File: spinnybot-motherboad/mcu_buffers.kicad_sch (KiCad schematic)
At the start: 15 parts, among them Q3 BC846, U4 ICM-20649, U5 ESP32-DEVKITC-32D, U6 SN74AHCT541DW, U7 SN74AHCT541DW

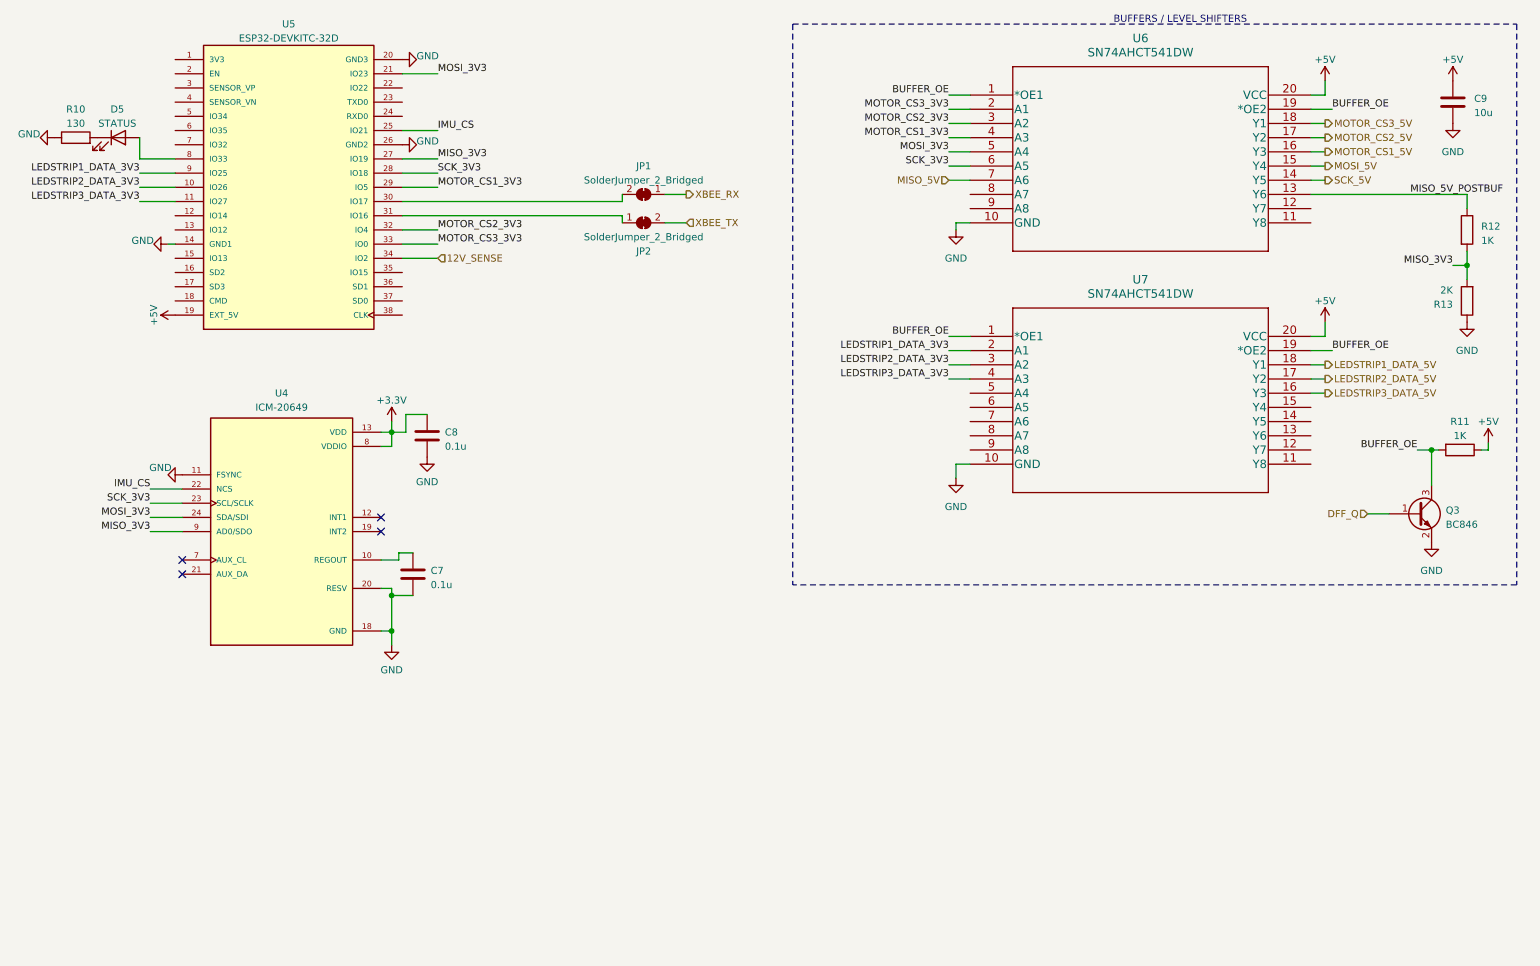
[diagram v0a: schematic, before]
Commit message: routed rev2 mainboard
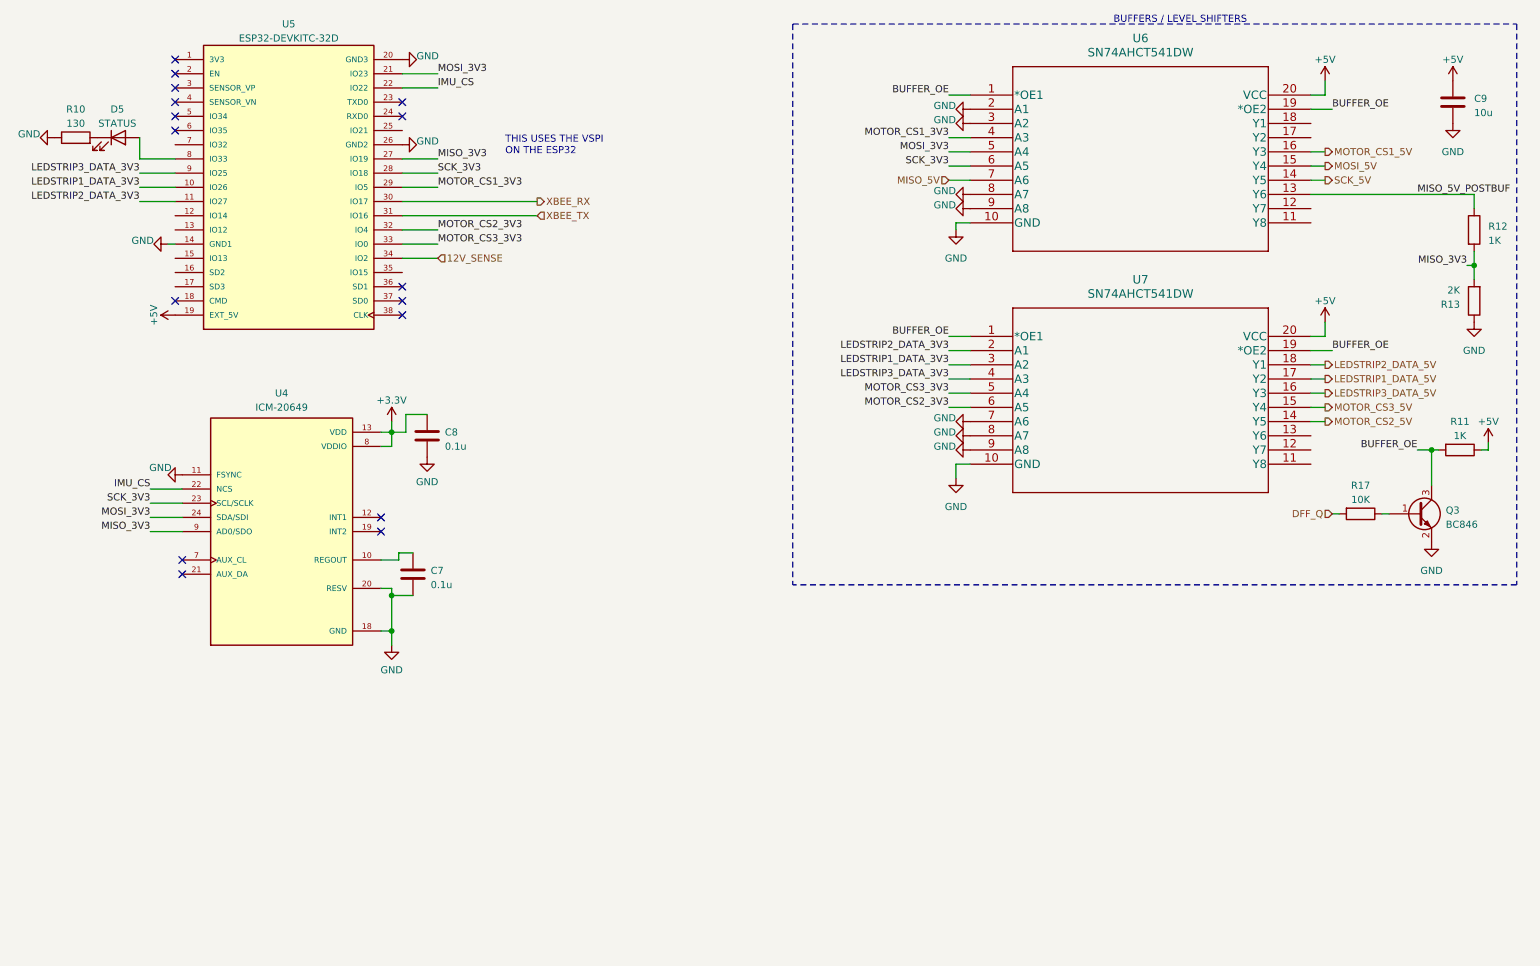
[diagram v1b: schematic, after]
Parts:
- removed JP1, JP2: SolderJumper_2_Bridged, Jumper:SolderJumper-2_P1.3mm_Open_RoundedPad1.0x1.5mm, symbol Jumper:SolderJumper_2_Bridged
- added R17: 10K, Resistor_SMD:R_0805_2012Metric_Pad1.20x1.40mm_HandSolder, symbol Device:R
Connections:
- net DFF_Q: now also R17.2; no longer Q3.1 (B)
- net GND: now also U6.2 (A1), U6.3 (A2), U6.8 (A7), U6.9 (A8), U7.7 (A6), U7.8 (A7), U7.9 (A8)
- net IMU_CS: now also U5.22 (IO22); no longer U5.25 (IO21)
- net LEDSTRIP1_DATA_3V3: now also U5.10 (IO26), U7.3 (A2); no longer U5.9 (IO25), U7.2 (A1)
- net LEDSTRIP1_DATA_5V: now also U7.17 (Y2); no longer U7.18 (Y1)
- net LEDSTRIP2_DATA_3V3: now also U5.11 (IO27), U7.2 (A1); no longer U5.10 (IO26), U7.3 (A2)
- net LEDSTRIP2_DATA_5V: now also U7.18 (Y1); no longer U7.17 (Y2)
- net LEDSTRIP3_DATA_3V3: now also U5.9 (IO25); no longer U5.11 (IO27)
- net MOTOR_CS2_3V3: now also U7.6 (A5); no longer U6.3 (A2)
- net MOTOR_CS2_5V: now also U7.14 (Y5); no longer U6.17 (Y2)
- net MOTOR_CS3_3V3: now also U7.5 (A4); no longer U6.2 (A1)
- net MOTOR_CS3_5V: now also U7.15 (Y4); no longer U6.18 (Y1)
- net XBEE_RX: now also U5.30 (IO17)
- net XBEE_TX: now also U5.31 (IO16)
- new net: Q3.1 (B), R17.1
- no-connect marks 4 -> 16
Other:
- note added: "THIS USES THE VSPI ON THE ESP32"
- moved on the sheet: R12, R13

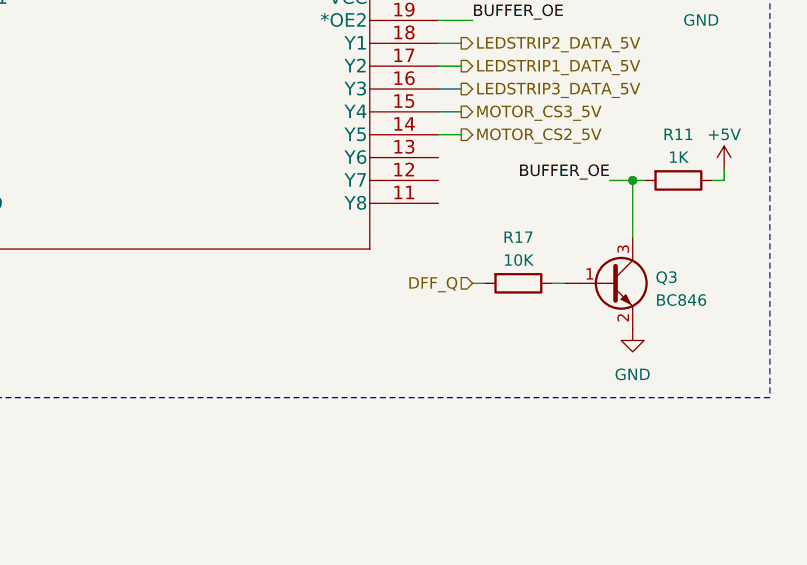
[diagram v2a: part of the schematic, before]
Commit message: split schematic into multiple files and stole Erick's homework on redoing the power button
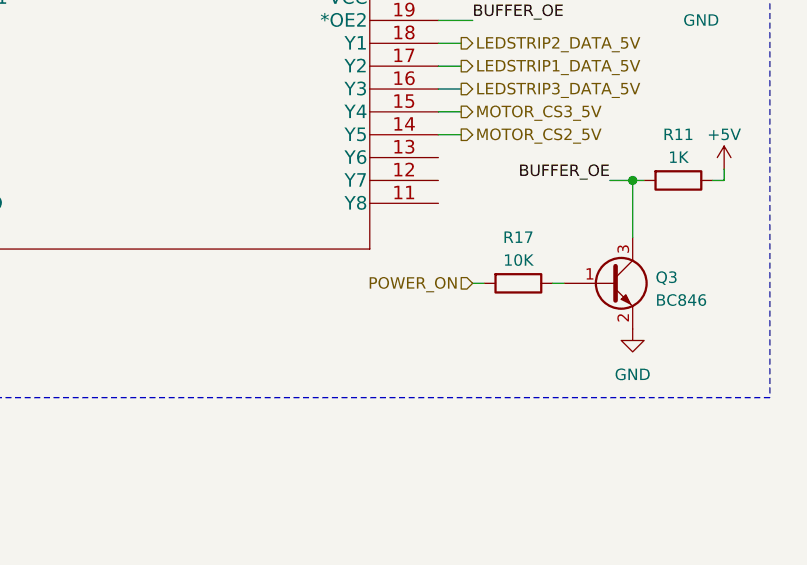
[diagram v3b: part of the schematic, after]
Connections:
- net DFF_Q renamed POWER_ON
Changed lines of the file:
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@@
-(kicad_sch (version 20210621) (generator eeschema)
+(kicad_sch (version 20211123) (generator eeschema)
   (paper "A4")
-  (junction (at 80.645 126.365) (diameter 1.016) (color 0 0 0 0))
-  (junction (at 274.32 60.96) (diameter 1.016) (color 0 0 0 0))
-  (junction (at 80.645 90.805) (diameter 1.016) (color 0 0 0 0))
-  (junction (at 266.7 93.98) (diameter 1.016) (color 0 0 0 0))
-  (junction (at 80.645 120.015) (diameter 1.016) (color 0 0 0 0))
+  (junction (at 266.7 93.98) (diameter 1.016) (color 0 0 0 0)
+  )
+  (junction (at 80.645 90.805) (diameter 1.016) (color 0 0 0 0)
+  )
+  (junction (at 274.32 60.96) (diameter 1.016) (color 0 0 0 0)
+  )
+  (junction (at 80.645 126.365) (diameter 1.016) (color 0 0 0 0)
+  )
+  (junction (at 80.645 120.015) (diameter 1.016) (color 0 0 0 0)
+  )
   (no_connect (at 82.55 64.77))
   (no_connect (at 82.55 67.31))
@@
     (effects (font (size 1.27 1.27)) (justify left))
   )
-  (hierarchical_label "DFF_Q" (shape input) (at 248.92 105.41 180)
+  (hierarchical_label "POWER_ON" (shape input) (at 248.92 105.41 180)
     (effects (font (size 1.27 1.27)) (justify right))
   )

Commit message: fixed some reference designators so the layout isn't broken
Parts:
- added U2: XBP9B-DMWTB002, XBP9-DMWTB002-XBEE-PRO-900HP:DIP2200W51P200L3294H279Q20P, symbol XBP9B-DMWTB002:XBP9B-DMWTB002
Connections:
- net +3V3: now also U2.1 (VCC)
- net GND: now also U2.10 (GND)
- net XBEE_RX: now also U2.3 (DIN/NCONFIG/DIO14)
- net XBEE_TX: now also U2.2 (DOUT/DIO13)
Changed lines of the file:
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@@
     (stroke (width 0) (type solid) (color 0 0 0 0))
+  )
+  (wire (pts (xy 158.75 175.26) (xy 156.21 175.26))
+    (stroke (width 0) (type default) (color 0 0 0 0))
   )
   (wire (pts (xy 180.34 76.2) (xy 184.15 76.2))
@@
     (stroke (width 0) (type solid) (color 0 0 0 0))
   )
+  (wire (pts (xy 158.75 134.62) (xy 156.21 134.62))
+    (stroke (width 0) (type default) (color 0 0 0 0))
+  )
   (wire (pts (xy 274.32 58.42) (xy 274.32 60.96))
     (stroke (width 0) (type solid) (color 0 0 0 0))
@@
     (stroke (width 0) (type solid) (color 0 0 0 0))
   )
+  (wire (pts (xy 158.75 177.8) (xy 158.75 175.26))
+    (stroke (width 0) (type default) (color 0 0 0 0))
+  )
   (wire (pts (xy 88.9 26.67) (xy 82.55 26.67))
     (stroke (width 0) (type solid) (color 0 0 0 0))
@@
     (stroke (width 0) (type solid) (color 0 0 0 0))
   )
+  (wire (pts (xy 158.75 130.81) (xy 158.75 134.62))
+    (stroke (width 0) (type default) (color 0 0 0 0))
+  )
   (text "BUFFERS / LEVEL SHIFTERS" (at 233.68 17.78 180)
     (effects (font (size 1.27 1.27)) (justify right bottom))
@@
     (effects (font (size 1.27 1.27)) (justify right bottom))
   )
+  (label "XBEE_RX" (at 100.33 147.32 180)
+    (effects (font (size 1.27 1.27)) (justify right bottom))
+  )
   (label "SCK_3V3" (at 37.465 103.505 180)
     (effects (font (size 1.27 1.27)) (justify right bottom))
@@
     (effects (font (size 1.27 1.27)) (justify left bottom))
   )
+  (label "XBEE_TX" (at 106.68 52.07 0)
+    (effects (font (size 1.27 1.27)) (justify left bottom))
+  )
   (label "BUFFER_OE" (at 264.16 93.98 180)
     (effects (font (size 1.27 1.27)) (justify right bottom))
@@
     (effects (font (size 1.27 1.27)) (justify right bottom))
   )
+  (label "XBEE_RX" (at 106.68 49.53 0)
+    (effects (font (size 1.27 1.27)) (justify left bottom))
+  )
   (label "MISO_5V_POSTBUF" (at 264.16 48.26 0)
     (effects (font (size 1.27 1.27)) (justify left bottom))
@@
     (effects (font (size 1.27 1.27)) (justify left bottom))
   )
+  (label "XBEE_TX" (at 100.33 144.78 180)
+    (effects (font (size 1.27 1.27)) (justify right bottom))
+  )
   (label "LEDSTRIP1_DATA_3V3" (at 180.34 78.74 180)
     (effects (font (size 1.27 1.27)) (justify right bottom))
@@
   )
   (hierarchical_label "MOTOR_CS2_5V" (shape output) (at 247.65 88.9 0)
-    (effects (font (size 1.27 1.27)) (justify left))
-  )
-  (hierarchical_label "XBEE_RX" (shape output) (at 106.68 49.53 0)
     (effects (font (size 1.27 1.27)) (justify left))
   )
@@
     (effects (font (size 1.27 1.27)) (justify right))
   )
-  (hierarchical_label "XBEE_TX" (shape input) (at 106.68 52.07 0)
-    (effects (font (size 1.27 1.27)) (justify left))
-  )
   (hierarchical_label "12V_SENSE" (shape input) (at 88.9 59.69 0)
     (effects (font (size 1.27 1.27)) (justify left))
@@
     )
     (property "Datasheet" "" (id 3) (at 247.65 71.12 0)
+      (effects (font (size 1.27 1.27)) hide)
+    )
+    (pin "1")
+  )
+  (symbol (lib_id "power:GND") (at 158.75 177.8 0) (unit 1)
+    (in_bom yes) (on_board yes) (fields_autoplaced)
+    (property "Reference" "#PWR0107" (id 0) (at 158.75 184.15 0)
+      (effects (font (size 1.27 1.27)) hide)
+    )
+    (property "Value" "GND" (id 1) (at 158.75 182.88 0))
+    (property "Footprint" "" (id 2) (at 158.75 177.8 0)
+      (effects (font (size 1.27 1.27)) hide)
+    )
+    (property "Datasheet" "" (id 3) (at 158.75 177.8 0)
       (effects (font (size 1.27 1.27)) hide)
     )
@@
     (pin "1")
   )
+  (symbol (lib_id "power:+3.3V") (at 158.75 130.81 0) (unit 1)
+    (in_bom yes) (on_board yes) (fields_autoplaced)
+    (property "Reference" "#PWR0106" (id 0) (at 158.75 134.62 0)
+      (effects (font (size 1.27 1.27)) hide)
+    )
+    (property "Value" "+3.3V" (id 1) (at 158.75 125.73 0))
+    (property "Footprint" "" (id 2) (at 158.75 130.81 0)
+      (effects (font (size 1.27 1.27)) hide)
+    )
+    (property "Datasheet" "" (id 3) (at 158.75 130.81 0)
+      (effects (font (size 1.27 1.27)) hide)
+    )
+    (pin "1")
+  )
   (symbol (lib_id "power:GND") (at 274.32 71.12 0) (unit 1)
     (in_bom yes) (on_board yes)
@@
     (pin "1")
   )
+  (symbol (lib_id "XBP9B-DMWTB002:XBP9B-DMWTB002") (at 128.27 154.94 0) (unit 1)
+    (in_bom yes) (on_board yes) (fields_autoplaced)
+    (property "Reference" "U2" (id 0) (at 128.27 127 0))
+    (property "Value" "XBP9B-DMWTB002" (id 1) (at 128.27 129.54 0))
+    (property "Footprint" "XBP9-DMWTB002-XBEE-PRO-900HP:DIP2200W51P200L3294H279Q20P" (id 2) (at 128.27 154.94 0)
+      (effects (font (size 1.27 1.27)) (justify left bottom) hide)
+    )
+    (property "Datasheet" "" (id 3) (at 128.27 154.94 0)
+      (effects (font (size 1.27 1.27)) (justify left bottom) hide)
+    )
+    (property "MANUFACTURER" "Digi International" (id 4) (at 128.27 154.94 0)
+      (effects (font (size 1.27 1.27)) (justify left bottom) hide)
+    )
+    (pin "1")
+    (pin "10")
+    (pin "11")
+    (pin "12")
+    (pin "13")
+    (pin "14")
+    (pin "15")
+    (pin "16")
+    (pin "17")
+    (pin "18")
+    (pin "19")
+    (pin "2")
+    (pin "20")
+    (pin "3")
+    (pin "4")
+    (pin "5")
+    (pin "6")
+    (pin "7")
+    (pin "9")
+  )
   (symbol (lib_id "SN74AHCT541DW:SN74AHCT541DW") (at 184.15 73.66 0) (unit 1)

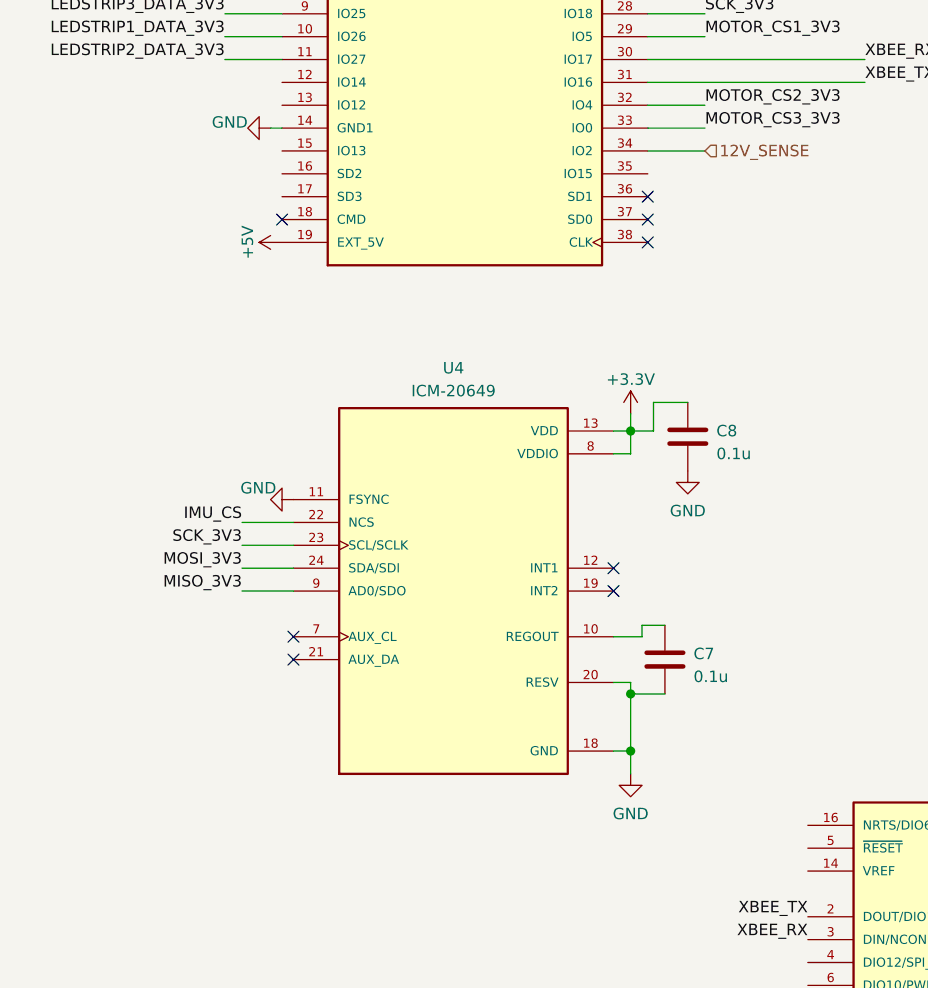
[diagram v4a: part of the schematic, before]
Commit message: add accelerometers, ADCs, and UART multiplexer
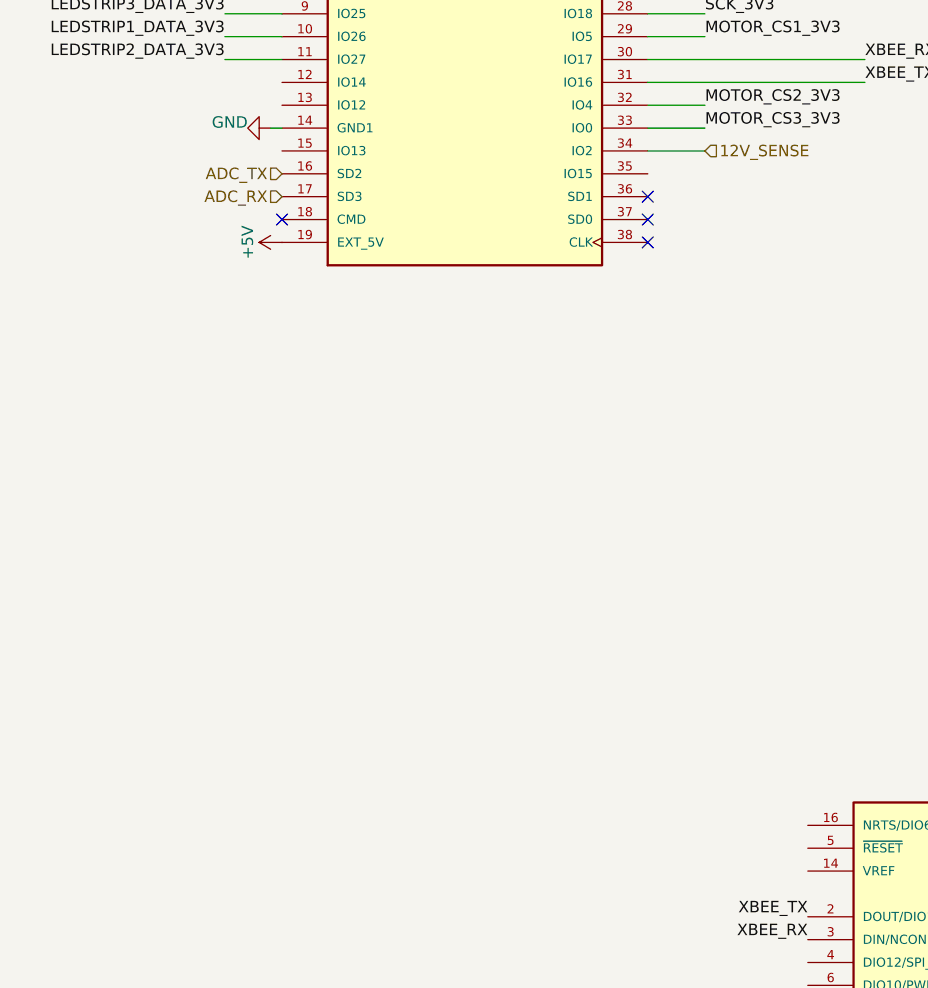
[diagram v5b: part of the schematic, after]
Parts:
- removed C7, C8: 0.1u, Capacitor_SMD:C_0805_2012Metric_Pad1.18x1.45mm_HandSolder, symbol Device:C
- removed U4: ICM-20649, icm-20649:QFN40P300X300X95-24N, symbol ICM-20649:ICM-20649
- U5: footprint NODEMCU_ESP32:MODULE_NODEMCU_ESP32 -> esp32-devkitc-32d:MODULE_ESP32-DEVKITC-32D
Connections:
- net ADC_TX: now reaches U5.16 (SD2)
- net ADC_RX: now reaches U5.17 (SD3)
- no-connect marks 16 -> 12
